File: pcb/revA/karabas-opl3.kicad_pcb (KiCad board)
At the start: 2 copper layers, 98.2 x 64 mm, 77 parts, among them J1 PJ307, J2 Conn_01x04, J4 Conn_02x30_Row_Letter_First, J5 Conn_02x05_Odd_Even, SW1 SW_DIP_x05, U1 UDA1334ATS, U15 1117-3.3, U2 1117-3.3, U21 74AHCT1G125DB, U3 EPM3128ATC100, U4 YMF262-M, X1 28.636MHz

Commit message: Updated references
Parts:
- added J5: 5V_PRG, Connector_PinHeader_2.54mm:PinHeader_1x02_P2.54mm_Vertical, F.Cu at (186.6, 84.0)
- C7: renamed from C33; footprint Capacitor_SMD:C_1206_3216Metric_Pad1.33x1.80mm_HandSolder -> Capacitor_SMD:C_0805_2012Metric_Pad1.18x1.45mm_HandSolder
- C9: renamed from C1; footprint Capacitor_SMD:C_1206_3216Metric_Pad1.33x1.80mm_HandSolder -> Capacitor_SMD:C_0805_2012Metric_Pad1.18x1.45mm_HandSolder
- moved LOGO1 54.0 mm to (113.2, 77.9)
- renumbered C29 to C1, C2 to C10, C49 to C11, C50 to C12, C52 to C13, C53 to C14, C54 to C15, C55 to C16, C58 to C17, C57 to C18, C60 to C19, C31 to C2, C61 to C20, C75 to C21, C62 to C22, C63 to C23, C64 to C24, C84 to C25, C5 to C26, C6 to C5, C7 to C6, C34 to C8, J5 to J1, J4 to J2, J1 to J3, J2 to J4, JP3 to JP1, LOGO2 to LOGO1, LOGO1 to LOGO2, R38 to R1, R72 to R10, R1 to R11, R4 to R12, R3 to R13, R2 to R14, R54 to R15, R55 to R16, R56 to R17, R57 to R18, R58 to R19, R52 to R2, R53 to R3, R41 to R4, R59 to R5, R42 to R6, R73 to R7, R90 to R8, R71 to R9, U4 to U1, U21 to U2, U1 to U4, U15 to U5, U2 to U6
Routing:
- net ~{RST}: track 62.2 -> 62.7 mm
- net ~{IORQ}: track 53.0 -> 53.5 mm
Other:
- board text added: "+"
- board text added: "ZX Spectrum OPL3 Soundcard"

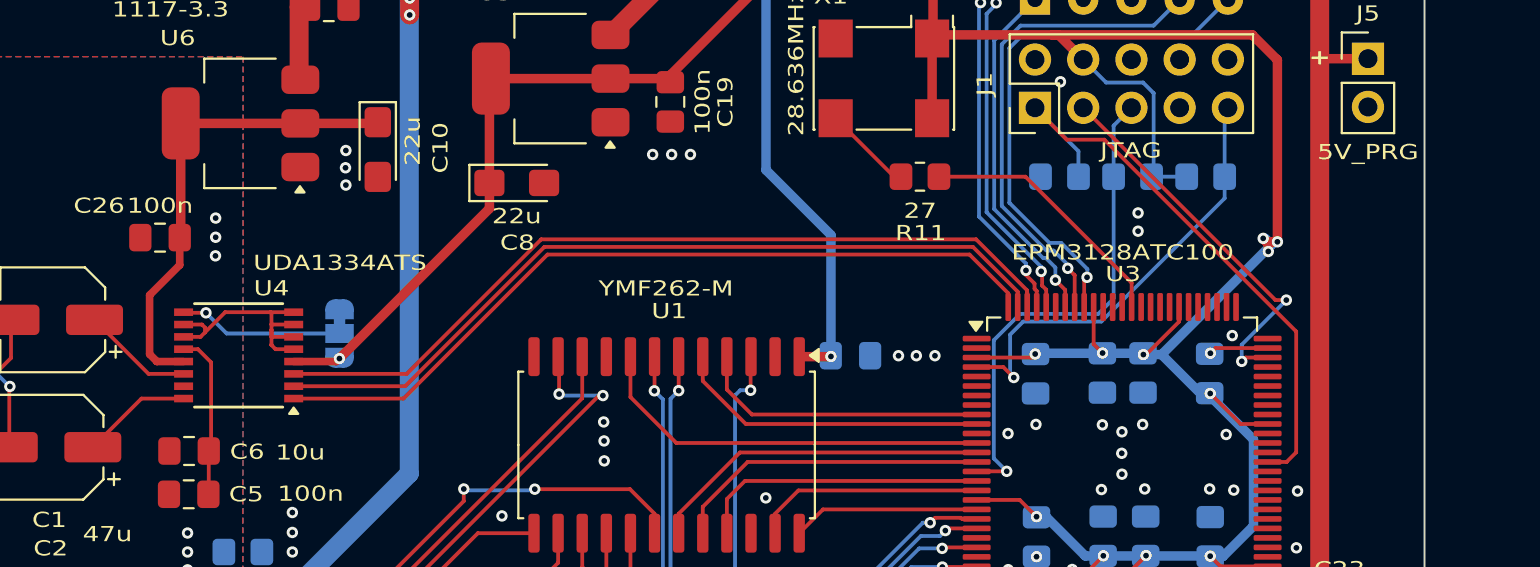
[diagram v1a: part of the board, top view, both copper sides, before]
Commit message: Added debug leds
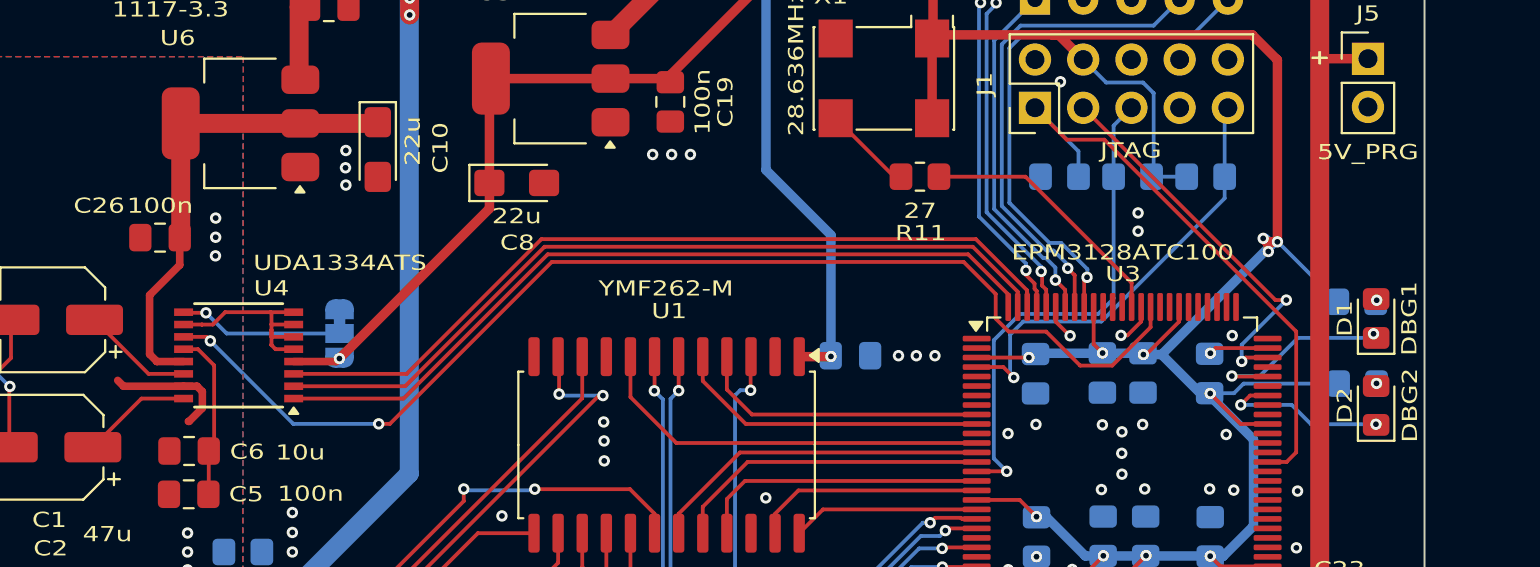
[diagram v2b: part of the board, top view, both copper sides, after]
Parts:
- added D1: DBG1, LED_SMD:LED_0805_2012Metric_Pad1.15x1.40mm_HandSolder, F.Cu at (187.1, 97.6)
- added D2: DBG2, LED_SMD:LED_0805_2012Metric_Pad1.15x1.40mm_HandSolder, F.Cu at (187.1, 102.2)
- added R20: 1k, Resistor_SMD:R_0805_2012Metric_Pad1.20x1.40mm_HandSolder, B.Cu at (186.0, 96.8)
- added R21: 1k, Resistor_SMD:R_0805_2012Metric_Pad1.20x1.40mm_HandSolder, B.Cu at (186.1, 101.1)
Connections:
- U3 pad 69: unconnected-(U3-I/O-Pad69) -> LED2
- U3 pad 71: unconnected-(U3-I/O-Pad71) -> LED1
- U3 pad 85: unconnected-(U3-I/O-Pad85) -> DAC_STD
- U4 pad 11: GND -> DAC_STD
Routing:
- net DAC_STD: track 0.00 -> 61.3 mm, vias 0 -> 2
- net +3V3: track 161.9 -> 173.3 mm
- net LED1: track 0.00 -> 10.6 mm, vias 0 -> 2
- net LED2: track 0.00 -> 9.20 mm, vias 0 -> 2
- net GNDA: track 0.00 -> 6.60 mm
- net GND: track 37.3 -> 39.5 mm, vias 78 -> 80
- net Net-(D2-A): track 0.00 -> 0.15 mm, vias 0 -> 1
- net Net-(D1-A): track 0.00 -> 0.10 mm, vias 0 -> 1
